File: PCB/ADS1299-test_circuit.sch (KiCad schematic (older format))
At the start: 93 parts, among them J1 CONN_01X07, P1 +5V, P10 CONN_01X03, P11 CONN_01X03, P12 CONN_01X03, P13 CONN_01X03, P14 BiasOut_C, P15 BiasOut_R, P16 BiasIn_C, P17 BiasIn_R, P19 Daisy, P20 Sw_pwdn, P21 Electrodes, P22 D/Ref, P23 -5V, P3 +3.3V, P4 +2.5V, P5 -2.5V, P6 CONN_01X03, P7 CONN_01X03, P8 CONN_01X03, P9 CONN_01X03, U1 REF5025, U2 REF5030, U3 ADS1299, U4 OPA735

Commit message: Agrego circuito revisado por Brian y lista de componentes. Falta comprar los capacitores para completar el circuito
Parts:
- removed C41: 1u, Capacitors_SMD:CP_Elec_5x5.3, symbol CP
- added C11, C44, C46, C6, C9: 0.1u, Capacitors_SMD:C_0805, symbol C
- added C41: 1u, Capacitors_SMD:C_0805, symbol C
- added C45: 10u, Capacitors_SMD:CP_Elec_4x4.5, symbol CP
- added P18, P2: CONN_01X01, Pin_Headers:Pin_Header_Straight_1x01_Pitch1.27mm, symbol CONN_01X01
- added R28, R29: 1, Resistors_SMD:R_0805, symbol R
- C1, C2: value 1u -> 10u
- C16, C17, C22, C28, C29, C34, C35: footprint Capacitors_SMD:C_0805 -> Capacitors_SMD:C_1206
- U1, U2: footprint Housings_SSOP:MSOP-8_3x3mm_Pitch0.65mm -> Housings_SOIC:SOIC-8-1EP_3.9x4.9mm_Pitch1.27mm
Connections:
- net +4.5 is gone; now on net +5: C2.1, U2.2 (IN)
- net +2.5: now also C9.1
- net +3.3: now also C11.1, C45.1
- net +5: now also C44.1, C46.1, C6.1
- net -2.5: now also C10.1, C41.1
- net -5: now also C8.1
- net GND: now also C11.2, C44.2, C45.2, C46.2, C6.2, C9.2
- net at C39.1, U3.55 (VCAP3): now also C41.2
- net at P4.1 (P1), R26.1, U1.6 (OUT): now also R28.1; no longer C5.1, C8.1
- net at P3.1 (P1), U2.6 (OUT): now also R29.1; no longer C10.1, C7.1
- net at U1.3 (TEMP): now also P2.1 (P1)
- net at U2.3 (TEMP): now also P18.1 (P1)
- new net: C5.1, R28.2
- new net: C7.1, R29.2
- no-connect marks 18 -> 17
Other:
- moved on the sheet: C1, C2, C3, C4, C5, C7, P1, P23

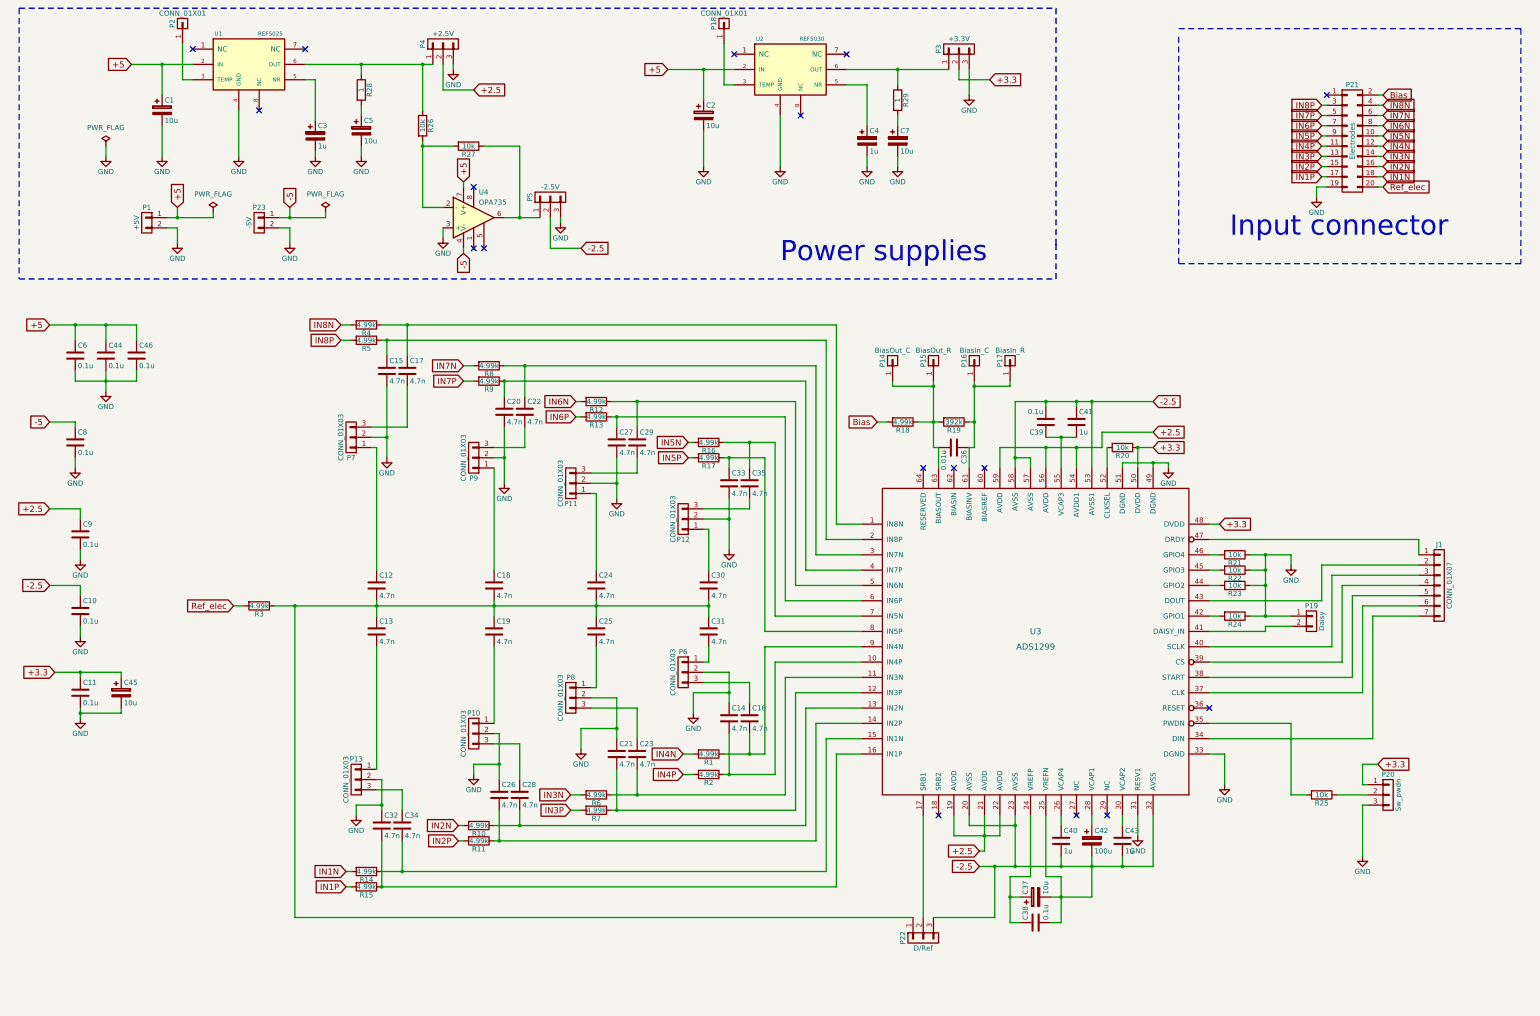
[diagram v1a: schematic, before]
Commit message: Circuito modificado de acuerdo al tamanio de los capacitores. Tira de pines invertidas
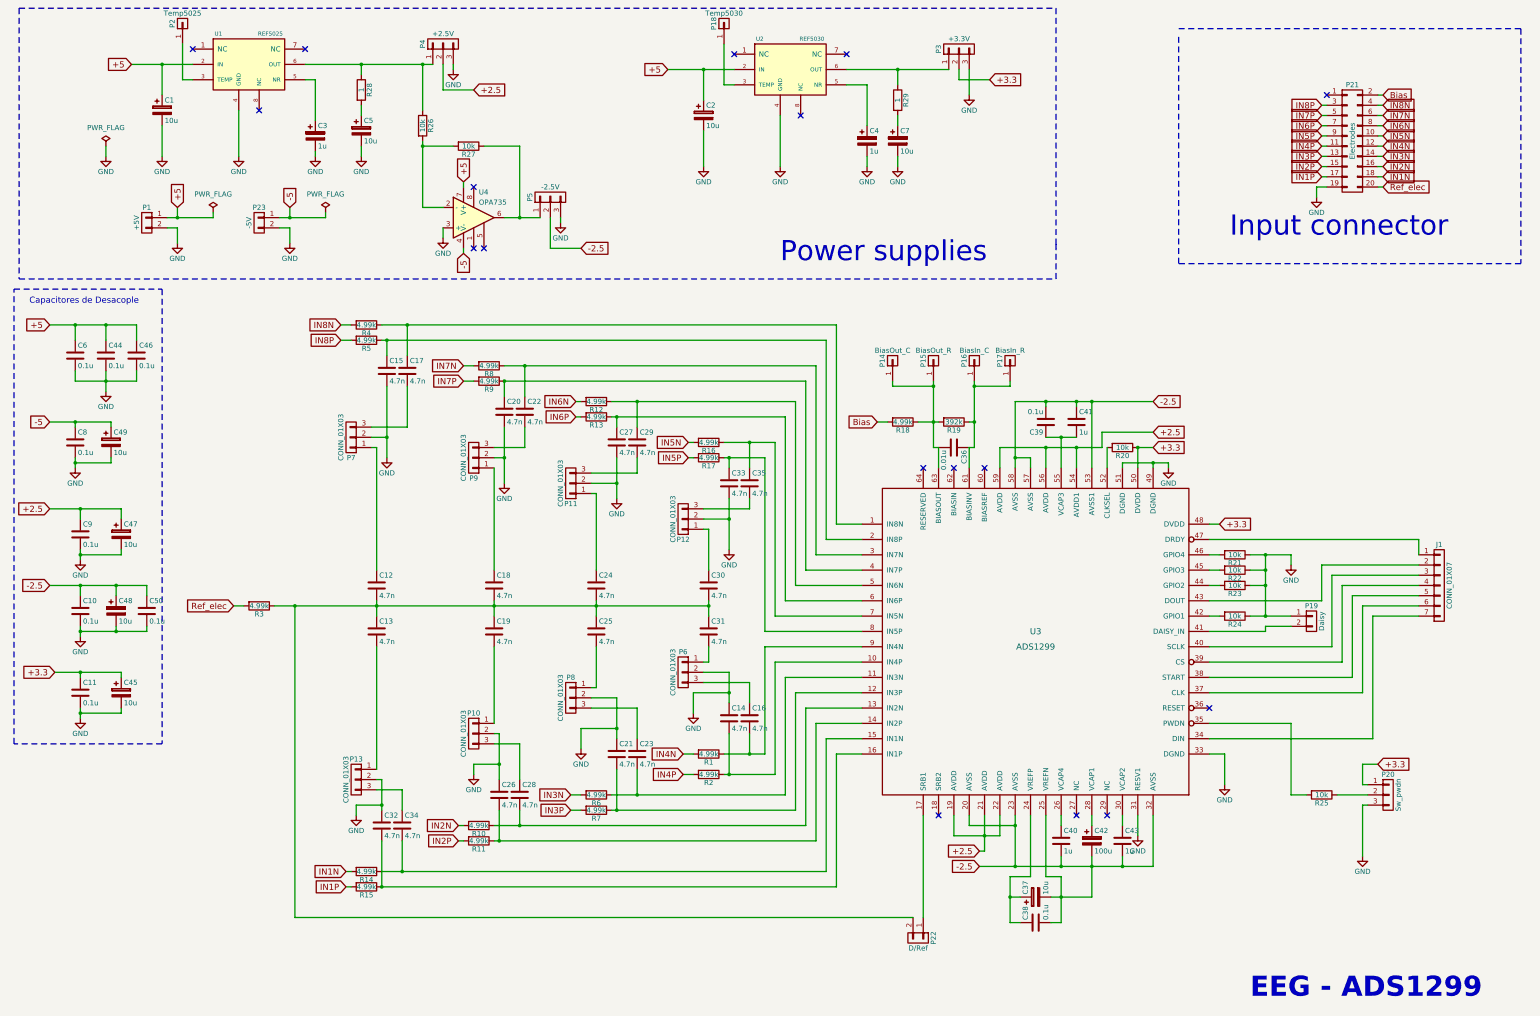
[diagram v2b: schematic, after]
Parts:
- removed P22: D/Ref, Pin_Headers:Pin_Header_Straight_1x03_Pitch2.54mm, symbol CONN_01X03
- added C47, C48, C49: 10u, Capacitors_SMD:CP_Elec_6.3x5.8, symbol CP
- added C50: 0.1u, Capacitors_SMD:C_0805, symbol C
- added P22: D/Ref, Pin_Headers:Pin_Header_Straight_1x02_Pitch2.54mm, symbol CONN_01X02
- C1, C2, C5, C7: footprint Capacitors_SMD:CP_Elec_6.3x4.5 -> Capacitors_SMD:CP_Elec_6.3x5.8
- C14, C15, C20, C21, C23, C26, C27, C32, C33, C41: footprint Capacitors_SMD:C_0805 -> Capacitors_SMD:C_1206
- C3, C4: footprint Capacitors_SMD:CP_Elec_6.3x4.5 -> Capacitors_SMD:CP_Elec_4x4.5
- C37, C42: footprint Capacitors_Tantalum_SMD:CP_Tantalum_Case-A_EIA-3216-18_Hand -> Capacitors_SMD:C_1206
- C45: footprint Capacitors_SMD:CP_Elec_4x4.5 -> Capacitors_SMD:CP_Elec_6.3x5.8
- J1: footprint Pin_Headers:Pin_Header_Straight_1x07_Pitch2.54mm_SMD_Pin1Left -> Pin_Headers:Pin_Header_Straight_1x07_Pitch2.54mm
- P18: value CONN_01X01 -> Temp5030
- P2: value CONN_01X01 -> Temp5025
- P21: footprint Pin_Headers:Pin_Header_Straight_2x10_Pitch2.54mm -> Pin_Headers_Mirrored:Pin_Header_Straight_2x10_Pitch2.54mm_Mirrored
- R21, R22, R23, R24, R25: footprint Resistors_SMD:R_0805 -> Resistors_SMD:R_1206
- U1, U2: footprint Housings_SOIC:SOIC-8-1EP_3.9x4.9mm_Pitch1.27mm -> Housings_SOIC:SOIC-8_3.9x4.9mm_Pitch1.27mm
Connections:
- net +2.5: now also C47.1
- net -2.5: now also C48.1, C50.1
- net -5: now also C49.1
- net GND: now also C47.2, C48.2, C49.2, C50.2
- net at U3.17 (SRB1): now also P22.1 (P1)
- net at C12.2, C13.1, C18.2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: now also P22.2 (P2)
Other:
- note added: "Capacitores de Desacople"
- note added: "EEG - ADS1299"

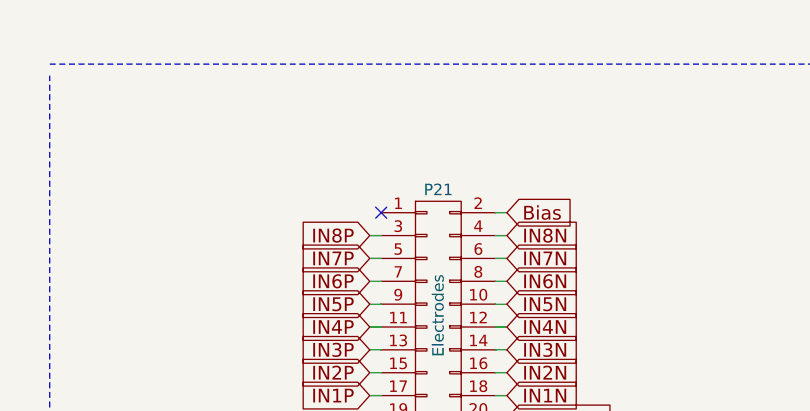
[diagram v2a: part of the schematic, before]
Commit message: Brian: ajustes del pcb. V1.0
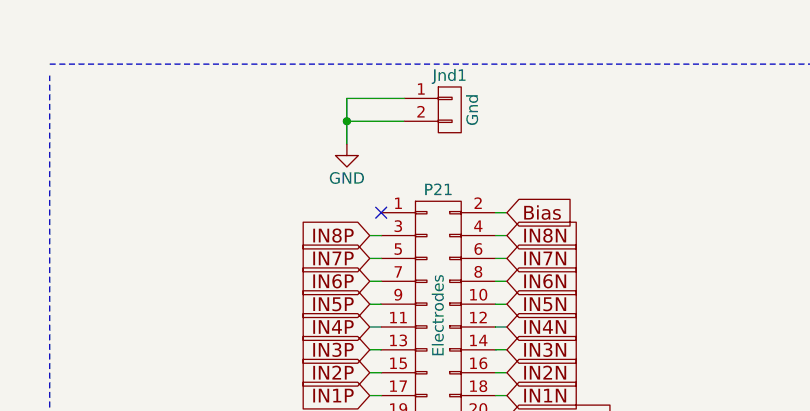
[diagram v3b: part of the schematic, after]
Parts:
- added Jnd1: Gnd, Pin_Headers:Pin_Header_Straight_1x02_Pitch2.54mm, symbol CONN_01X02
- C37, C42: footprint Capacitors_SMD:C_1206 -> Capacitors_THT:CP_Radial_Tantal_D5.0mm_P2.50mm
- C41: footprint Capacitors_SMD:C_1206 -> Capacitors_SMD:C_0805
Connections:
- net GND: now also Jnd1.1 (P1), Jnd1.2 (P2)

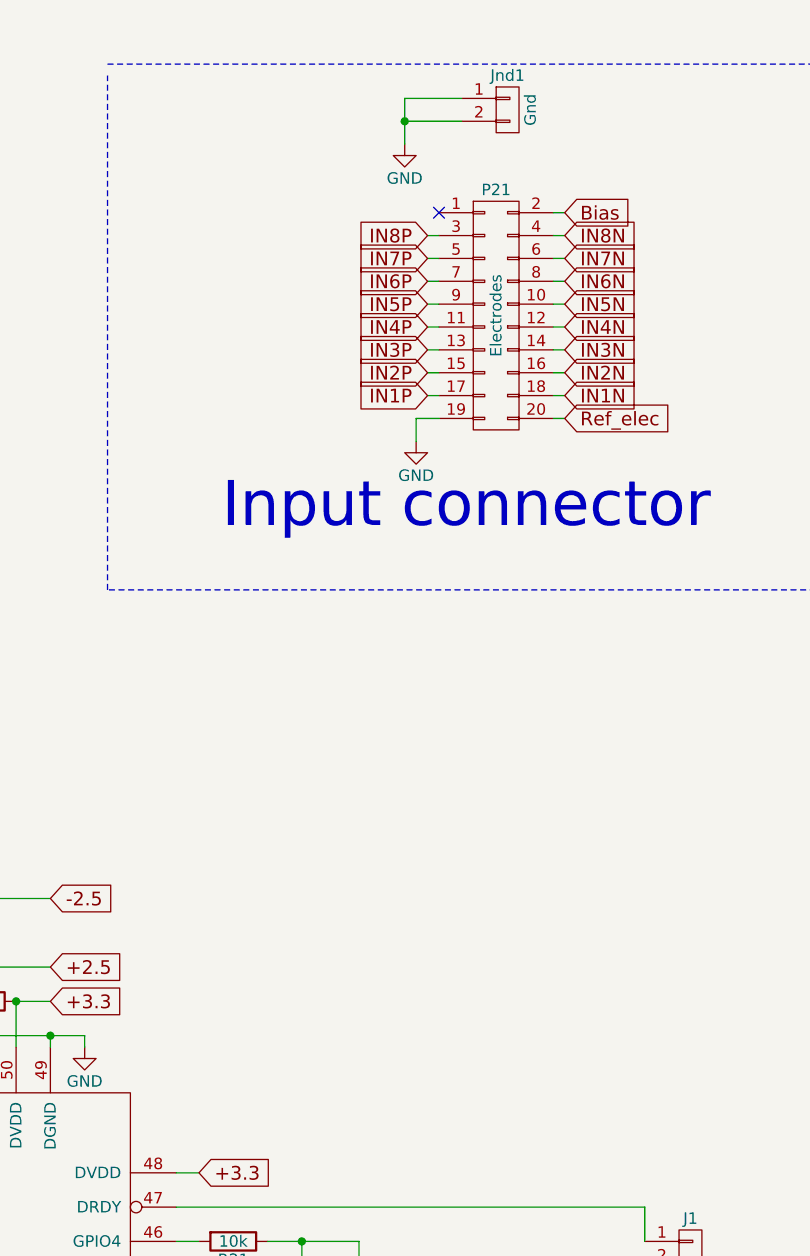
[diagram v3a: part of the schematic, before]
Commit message: Agrego pines torneados para GND, logo fiuba y acomodo pistas
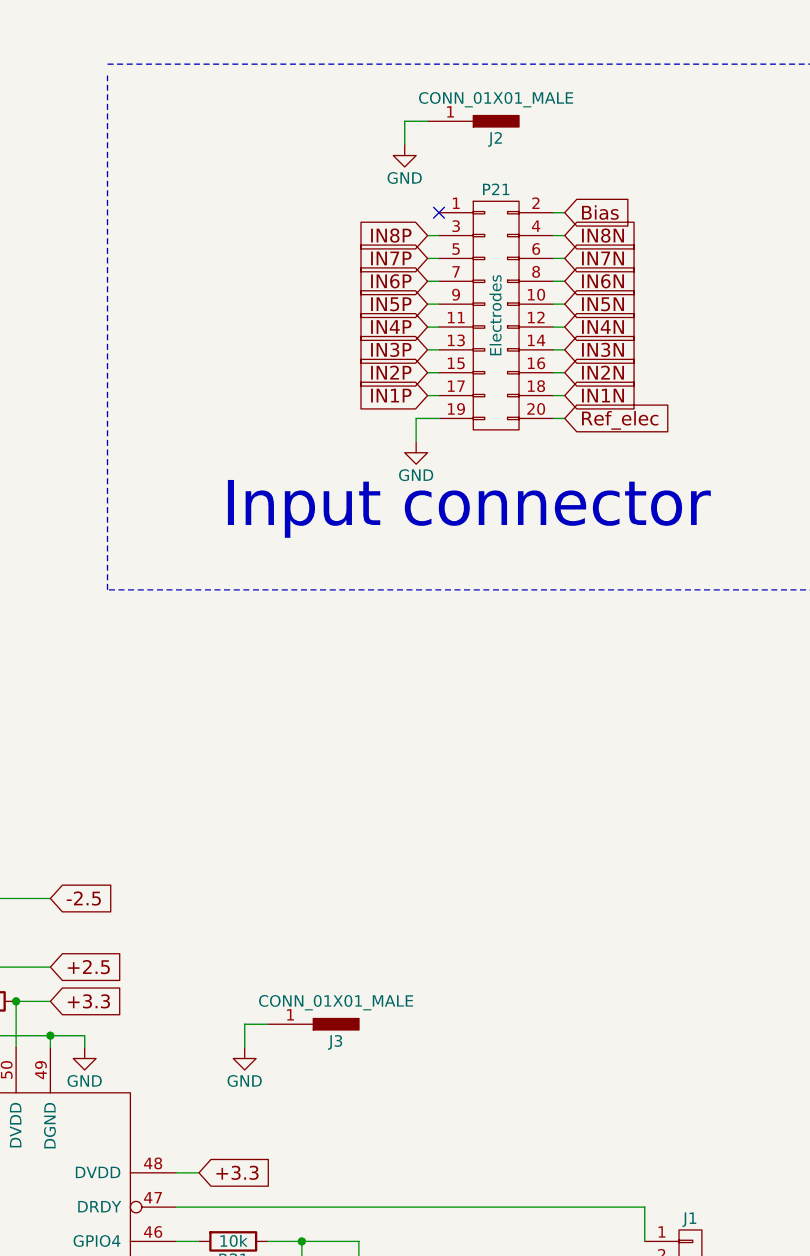
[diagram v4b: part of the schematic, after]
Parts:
- removed Jnd1: Gnd, Pin_Headers:Pin_Header_Straight_1x02_Pitch2.54mm, symbol CONN_01X02
- added J2, J3: CONN_01X01_MALE, PINtorneado:PINtorneado, symbol CONN_01X01_MALE
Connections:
- net GND: now also J2.1, J3.1

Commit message: Update Arduino and matlab code
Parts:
- added J10, J11, J12, J13, J14, J15, J16, J17, J18, J19, J20, J21, J22, J23, J24, J25, J26, J27, J28, J29, J30, J31, J32, J33, J4, J5, J6, J7, J8, J9: Via, Pin_Headers:Pin_Header_Straight_1x01_Pitch2.54mm, symbol CONN_01X01
- J1: value CONN_01X07 -> OUT
- J2, J3: value CONN_01X01_MALE -> GND
- P10: value CONN_01X03 -> IN2
- P11: value CONN_01X03 -> IN6
- P12: value CONN_01X03 -> IN5
- P13: value CONN_01X03 -> IN1
- P18, P2: footprint Pin_Headers:Pin_Header_Straight_1x01_Pitch1.27mm -> Pin_Headers:Pin_Header_Straight_1x01_Pitch2.54mm
- P21: footprint Pin_Headers_Mirrored:Pin_Header_Straight_2x10_Pitch2.54mm_Mirrored -> Pin_Headers:Pin_Header_Straight_2x10_Pitch2.54mm
- P6: value CONN_01X03 -> IN4
- P7: value CONN_01X03 -> IN8
- P8: value CONN_01X03 -> IN3
- P9: value CONN_01X03 -> IN7
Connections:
- net GND: now also J10.1 (P1), J11.1 (P1), J12.1 (P1), J13.1 (P1), J14.1 (P1), J15.1 (P1), J16.1 (P1), J17.1 (P1), J18.1 (P1), J19.1 (P1), J20.1 (P1), J21.1 (P1), J22.1 (P1), J23.1 (P1), J24.1 (P1), J25.1 (P1), J26.1 (P1), J27.1 (P1), J28.1 (P1), J29.1 (P1), J30.1 (P1), J31.1 (P1), J32.1 (P1), J33.1 (P1), J4.1 (P1), J5.1 (P1), J6.1 (P1), J7.1 (P1), J8.1 (P1), J9.1 (P1)
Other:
- note added: "VIAS"
- moved on the sheet: J2, J3, P21
